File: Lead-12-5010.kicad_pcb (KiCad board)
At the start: 2 copper layers, 196.1 x 42.5 mm, 54 parts, among them Q1 2N3904, U1 TL082

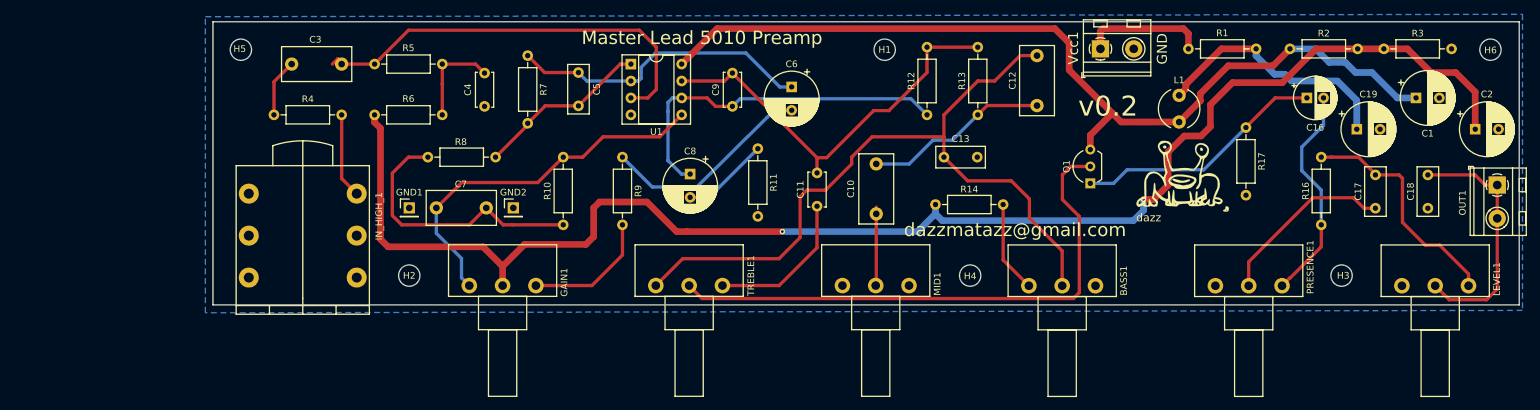
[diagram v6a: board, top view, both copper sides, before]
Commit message: Removed low input. Restored output buffer. JST connectors used instead of terminal blocks.
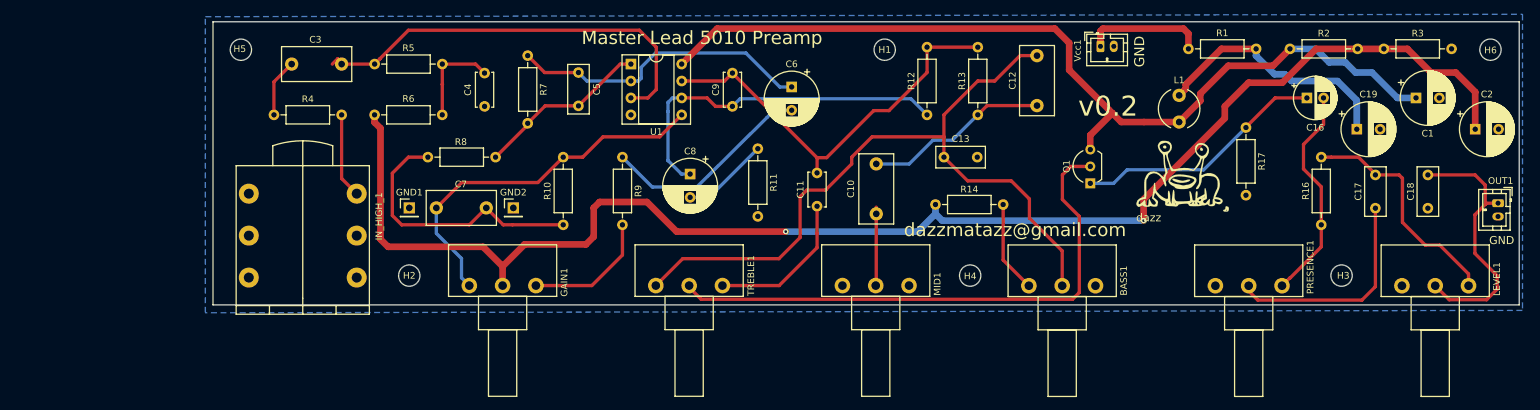
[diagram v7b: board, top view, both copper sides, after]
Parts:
- OUT1, Vcc1: footprint TerminalBlock_MetzConnect:TerminalBlock_MetzConnect_Type094_RT03502HBLU_1x02_P5.00mm_Horizontal -> Connector_JST:JST_PH_B2B-PH-K_1x02_P2.00mm_Vertical
- moved OUT1 2.72 mm to (267.3, 116.1)
- moved Vcc1 0.38 mm to (207.6, 92.6)
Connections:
- OUT1 pad 2: Net-(C18-Pad1) -> GND
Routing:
- net Net-(C17-Pad2): track 27.2 -> 33.0 mm
- net Vref: track 224.0 -> 221.1 mm
- net Net-(C18-Pad1): track 37.5 -> 39.7 mm
